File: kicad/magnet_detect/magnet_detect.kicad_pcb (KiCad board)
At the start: 2 copper layers, 28 x 28 mm, 8 parts, among them J1 Conn_01x06_Socket, U1 AS5047D

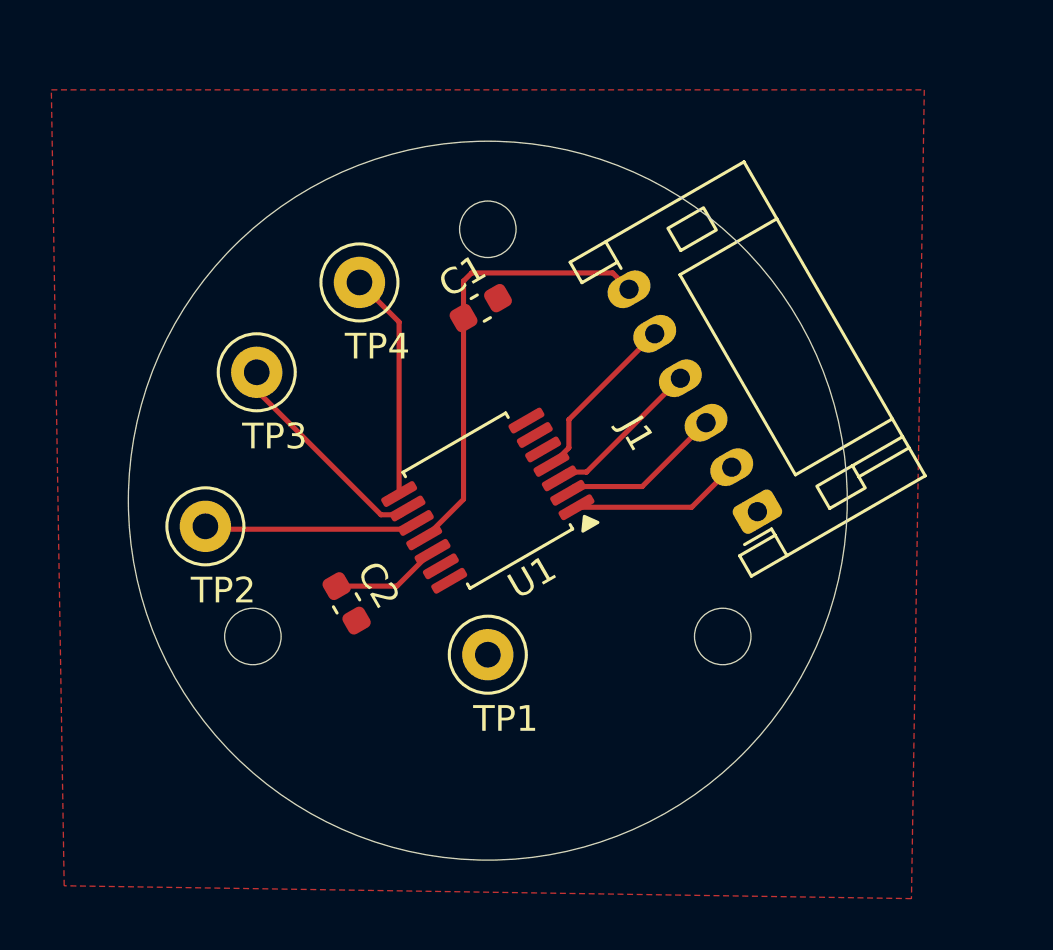
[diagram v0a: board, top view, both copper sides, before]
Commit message: fix(kicad):esp32_magnet
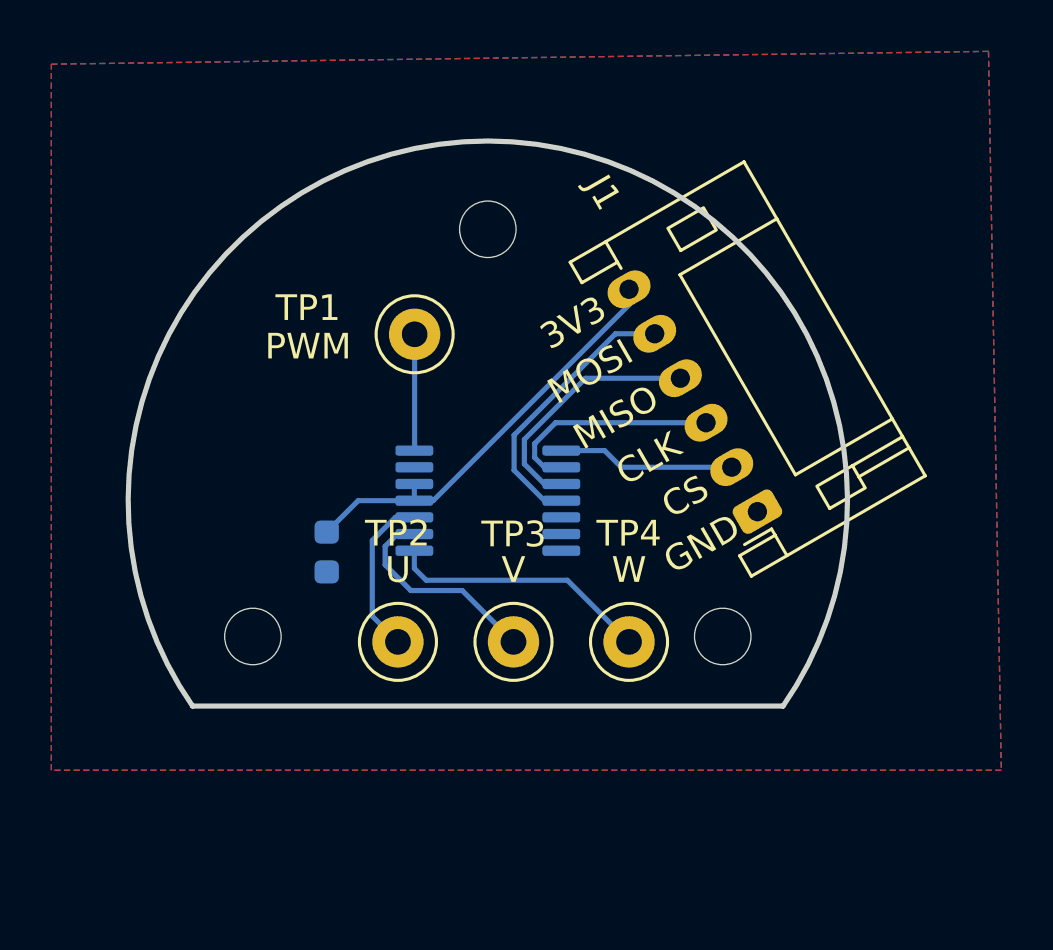
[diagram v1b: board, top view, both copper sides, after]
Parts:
- removed C2: 1uF, Capacitor_SMD:C_0603_1608Metric
- C1, U1: moved to B.Cu
- moved TP4 17.5 mm to (140.0, 127.0)
- moved TP3 14.5 mm to (135.5, 127.0)
- moved TP1 12.8 mm to (131.6, 115.0)
- moved C1 11.2 mm to (128.2, 123.5), turned to -90 degrees
- moved TP2 8.75 mm to (131.0, 127.0)
- turned U1 to 180 degrees
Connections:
- C1 pad 1: +5V -> +3.3V
- J1 pad 6: +5V -> +3.3V
- U1 pad 11: +5V -> +3.3V
- U1 pad 12: Net-(U1-VDD3V3) -> +3.3V
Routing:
- net +5V: track 17.5 -> 0.00 mm
- net +3.3V: track 0.00 -> 16.7 mm
- net Net-(U1-I/PWM): track 0.00 -> 4.52 mm
- net Net-(U1-VDD3V3): track 4.27 -> 0.00 mm
- net Net-(J1-Pin_5): track 6.75 -> 10.8 mm
- net Net-(J1-Pin_4): track 6.31 -> 9.78 mm
- net Net-(J1-Pin_3): track 6.50 -> 8.75 mm
- net Net-(U1-U): track 8.34 -> 6.37 mm
- net Net-(U1-W/PWM): track 8.88 -> 10.2 mm
- added copper zone on B.Cu, net GNDD
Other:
- board size 28 x 28 mm -> 28 x 22 mm
- board text added: "3V3"
- board text added: "CLK"
- board text added: "CS"
- board text added: "GND"
- board text added: "MISO"
- board text added: "MOSI"
